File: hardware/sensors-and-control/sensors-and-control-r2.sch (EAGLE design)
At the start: 138 parts, among them IC1 STM32L496ZET6

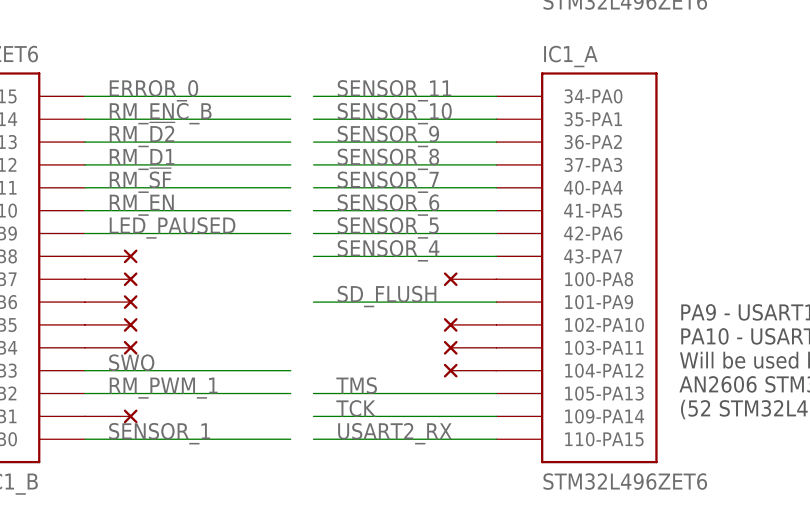
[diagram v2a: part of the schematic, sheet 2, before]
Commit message: - moved SD_FLUSH to A8
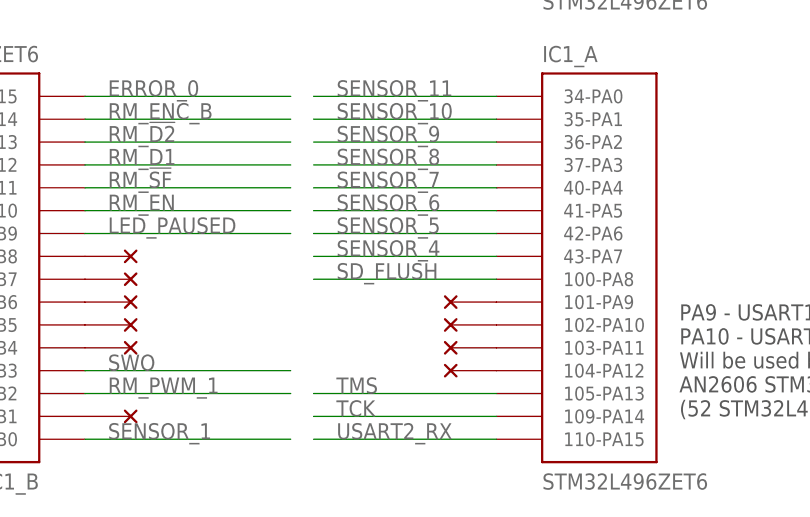
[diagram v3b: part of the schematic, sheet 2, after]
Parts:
- removed U$28: NC, voltage-ground:NC
- added U$12: NC, voltage-ground:NC
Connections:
- removed net N$44: IC1_A.100-PA8, U$28.1
- new net N$28: IC1_A.101-PA9, U$12.1
- net SD_FLUSH: now also IC1_A.100-PA8; no longer IC1_A.101-PA9
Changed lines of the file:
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@@
 <part name="U$26" library="voltage-ground" library_urn="urn:adsk.eagle:library:704746" deviceset="NC" device=""/>
 <part name="U$27" library="voltage-ground" library_urn="urn:adsk.eagle:library:704746" deviceset="NC" device=""/>
-<part name="U$28" library="voltage-ground" library_urn="urn:adsk.eagle:library:704746" deviceset="NC" device=""/>
 <part name="U$31" library="voltage-ground" library_urn="urn:adsk.eagle:library:704746" deviceset="NC" device=""/>
 <part name="U$32" library="voltage-ground" library_urn="urn:adsk.eagle:library:704746" deviceset="NC" device=""/>
@@
 <part name="R32" library="resistors" library_urn="urn:adsk.eagle:library:704770" deviceset="RESISTOR_0.1W" device="" package3d_urn="urn:adsk.eagle:package:704947/3" value="47k"/>
 <part name="SUPPLY14" library="voltage-ground" library_urn="urn:adsk.eagle:library:704746" deviceset="+3.3V" device=""/>
+<part name="U$12" library="voltage-ground" library_urn="urn:adsk.eagle:library:704746" deviceset="NC" device=""/>
 </parts>
 <sheets>
@@
 <instance part="U$26" gate="G$1" x="73.66" y="76.2" rot="R180"/>
 <instance part="U$27" gate="G$1" x="73.66" y="73.66" rot="R180"/>
-<instance part="U$28" gate="G$1" x="73.66" y="38.1" rot="R180"/>
 <instance part="U$31" gate="G$1" x="33.02" y="38.1"/>
 <instance part="U$32" gate="G$1" x="33.02" y="40.64"/>
@@
 <instance part="R32" gate="G$1" x="170.18" y="68.58" rot="R90"/>
 <instance part="SUPPLY14" gate="G$1" x="185.42" y="78.74"/>
+<instance part="U$12" gate="G$1" x="73.66" y="35.56" rot="R180"/>
 </instances>
 <busses>
@@
 </segment>
 </net>
-<net name="N$44" class="0">
-<segment>
-<pinref part="IC1" gate="_A" pin="100-PA8"/>
-<pinref part="U$28" gate="G$1" pin="1"/>
-</segment>
-</net>
 <net name="N$47" class="0">
 <segment>
@@
 </segment>
 </net>
-<net name="SD_FLUSH" class="0">
-<segment>
-<pinref part="IC1" gate="_A" pin="101-PA9"/>
-<wire x1="76.2" y1="35.56" x2="55.88" y2="35.56" width="0.1524" layer="91"/>
-<label x="58.42" y="35.56" size="1.778" layer="95"/>
-</segment>
-</net>
 <net name="N$35" class="0">
 <segment>
@@
 </segment>
 </net>
+<net name="SD_FLUSH" class="0">
+<segment>
+<pinref part="IC1" gate="_A" pin="100-PA8"/>
+<wire x1="76.2" y1="38.1" x2="55.88" y2="38.1" width="0.1524" layer="91"/>
+<label x="58.42" y="38.1" size="1.778" layer="95"/>
+</segment>
+</net>
+<net name="N$28" class="0">
+<segment>
+<pinref part="IC1" gate="_A" pin="101-PA9"/>
+<pinref part="U$12" gate="G$1" pin="1"/>
+</segment>
+</net>
